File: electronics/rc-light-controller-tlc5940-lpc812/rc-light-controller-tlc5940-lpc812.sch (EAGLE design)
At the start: 41 parts, among them U2 TLC5940PWP

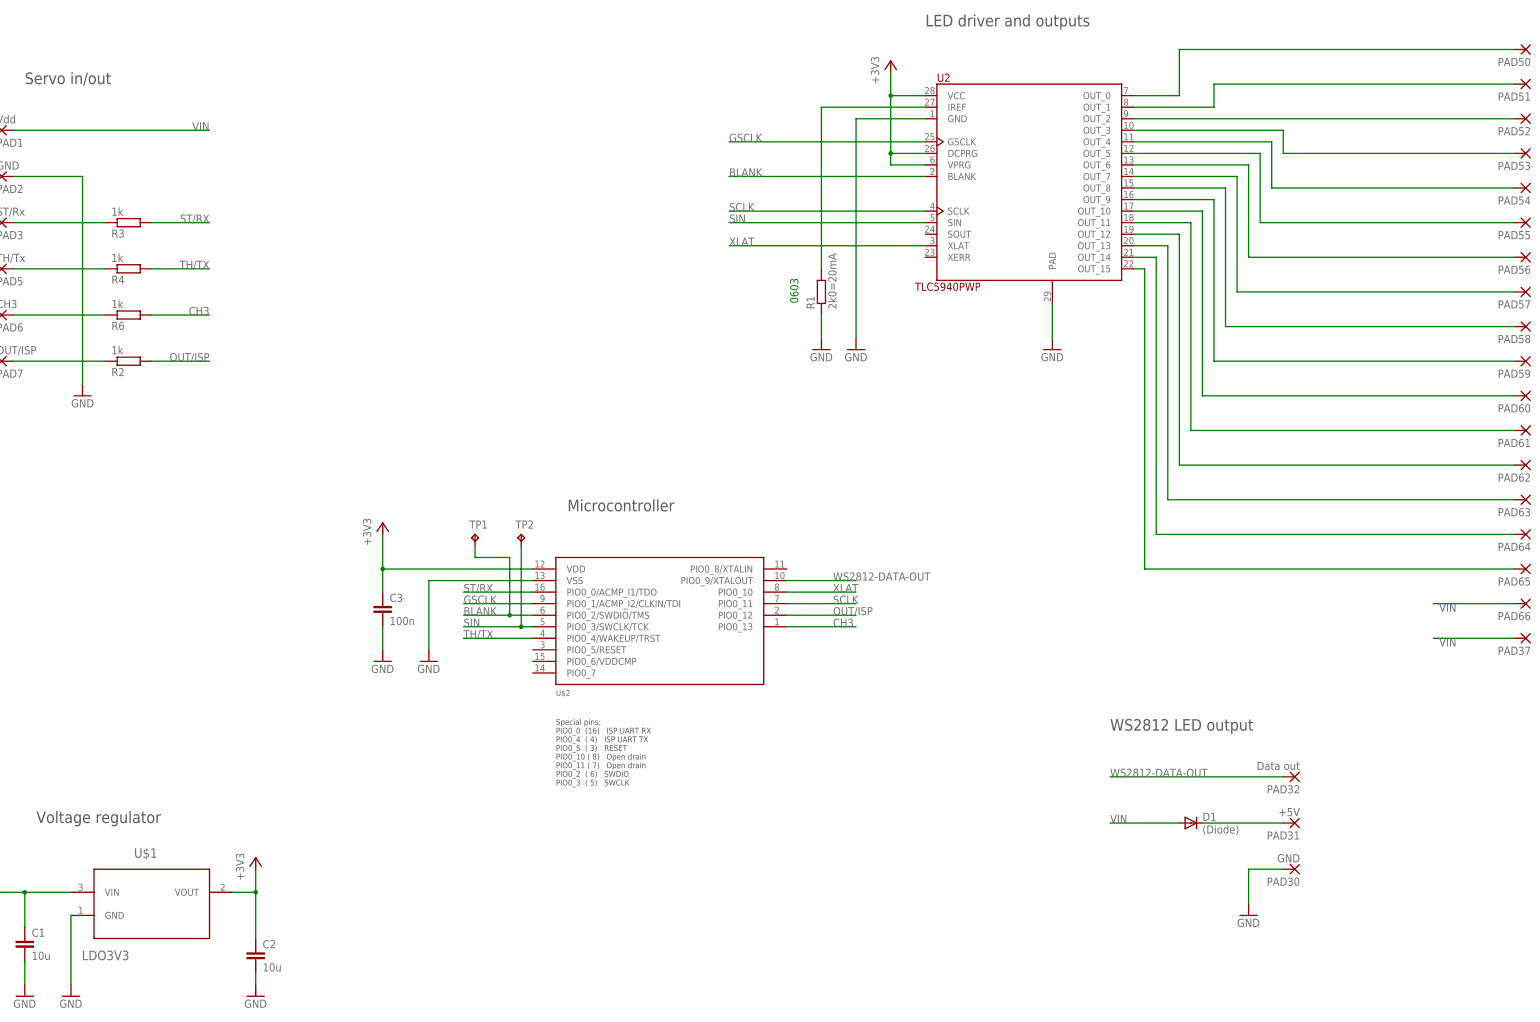
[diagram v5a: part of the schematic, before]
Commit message: Add reset test pad, tweak silk screen and vias
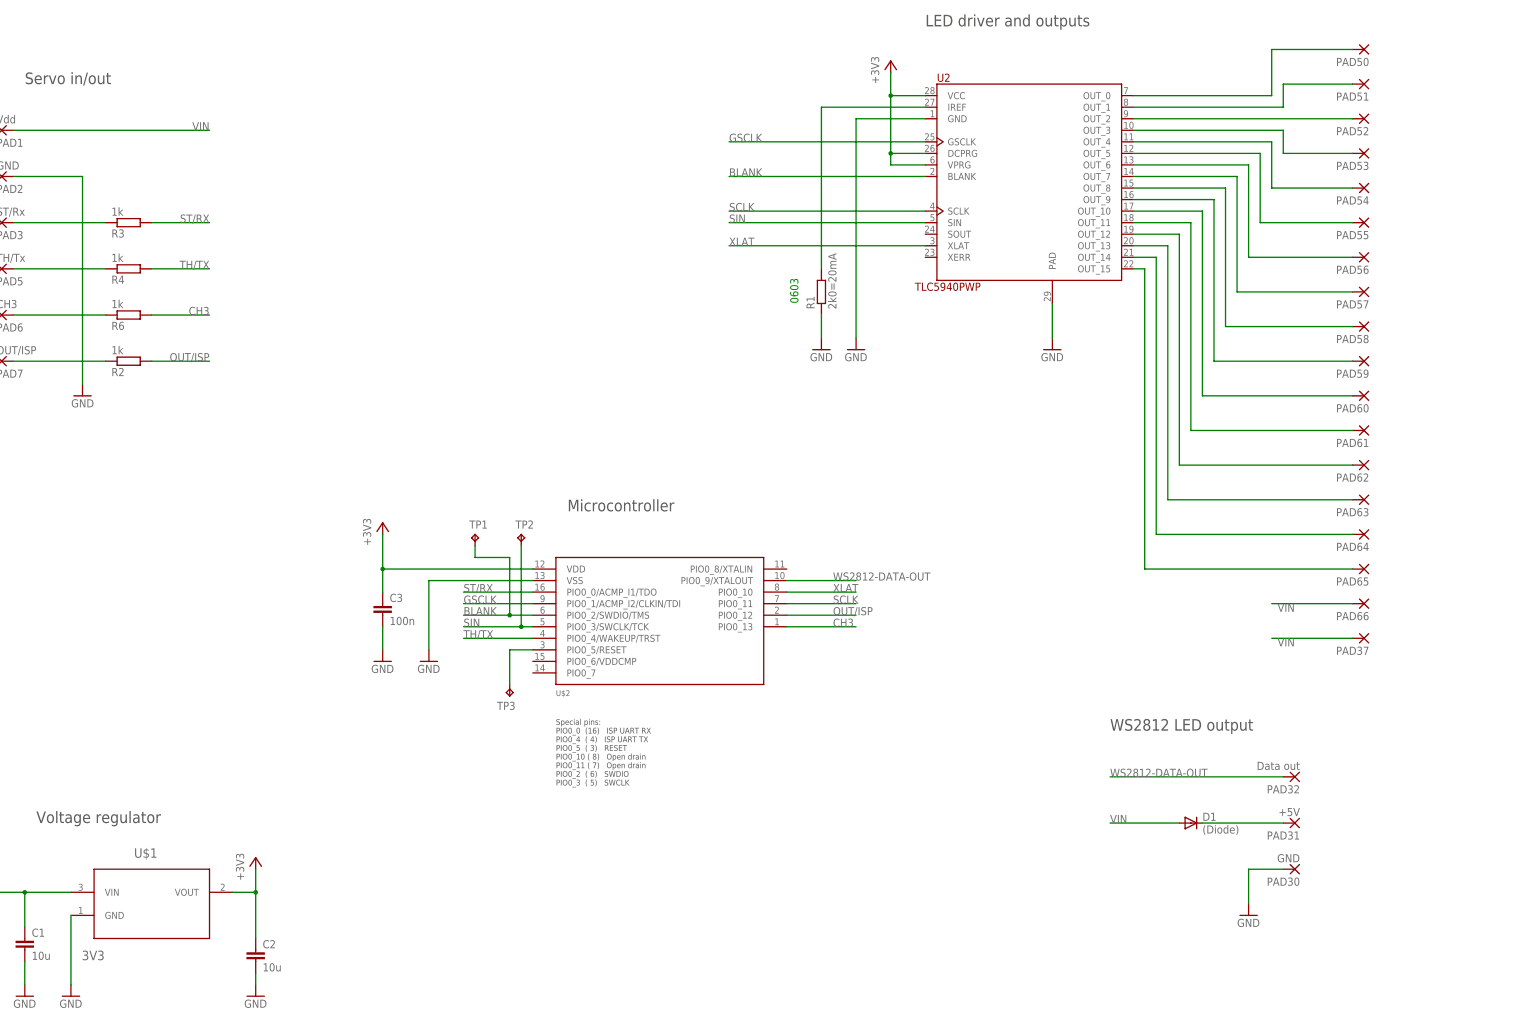
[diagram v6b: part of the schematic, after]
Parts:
- added TP3: RESET, testpad:TPTP10R
- U$1: value LDO3V3 -> 3V3
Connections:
- new net N$4: TP3.TP, U$2.PIO0_5/RESET
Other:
- moved on the sheet: PAD37, PAD50, PAD51, PAD52, PAD53, PAD54, PAD55, PAD56, PAD57, PAD58, PAD59, PAD60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

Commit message: Update board pin assignment to avoid using open drain pins
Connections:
- net BLANK: now also U$2.PIO0_6/VDDCMP; no longer TP1.TP, U$2.PIO0_2/SWDIO/TMS
- net SCLK: now also TP2.TP, U$2.PIO0_3/SWCLK/TCK; no longer U$2.PIO0_11
- net SIN: now also U$2.PIO0_7; no longer TP2.TP, U$2.PIO0_3/SWCLK/TCK
- net XLAT: now also TP1.TP, U$2.PIO0_2/SWDIO/TMS; no longer U$2.PIO0_10
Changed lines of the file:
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@@
 </segment>
 <segment>
-<pinref part="U$2" gate="G$1" pin="PIO0_3/SWCLK/TCK"/>
-<wire x1="152.4" y1="114.3" x2="149.86" y2="114.3" width="0.1524" layer="91"/>
-<label x="137.16" y="114.3" size="1.778" layer="95"/>
-<wire x1="149.86" y1="114.3" x2="137.16" y2="114.3" width="0.1524" layer="91"/>
-<wire x1="149.86" y1="114.3" x2="149.86" y2="132.08" width="0.1524" layer="91"/>
-<junction x="149.86" y="114.3"/>
-<pinref part="TP2" gate="G$1" pin="TP"/>
+<wire x1="152.4" y1="104.14" x2="137.16" y2="104.14" width="0.1524" layer="91"/>
+<label x="137.16" y="104.14" size="1.778" layer="95"/>
+<pinref part="U$2" gate="G$1" pin="PIO0_7"/>
 </segment>
 </net>
@@
 </segment>
 <segment>
-<wire x1="208.28" y1="119.38" x2="223.52" y2="119.38" width="0.1524" layer="91"/>
-<pinref part="U$2" gate="G$1" pin="PIO0_11"/>
-<label x="218.44" y="119.38" size="1.778" layer="95"/>
+<label x="137.16" y="114.3" size="1.778" layer="95"/>
+<wire x1="149.86" y1="114.3" x2="137.16" y2="114.3" width="0.1524" layer="91"/>
+<pinref part="U$2" gate="G$1" pin="PIO0_3/SWCLK/TCK"/>
+<wire x1="152.4" y1="114.3" x2="149.86" y2="114.3" width="0.1524" layer="91"/>
+<wire x1="149.86" y1="114.3" x2="149.86" y2="132.08" width="0.1524" layer="91"/>
+<pinref part="TP2" gate="G$1" pin="TP"/>
+<junction x="149.86" y="114.3"/>
 </segment>
 </net>
 <net name="XLAT" class="0">
 <segment>
-<pinref part="U$2" gate="G$1" pin="PIO0_10"/>
-<wire x1="208.28" y1="121.92" x2="223.52" y2="121.92" width="0.1524" layer="91"/>
-<label x="218.44" y="121.92" size="1.778" layer="95"/>
+<label x="137.16" y="116.84" size="1.778" layer="95"/>
+<wire x1="147.32" y1="116.84" x2="137.16" y2="116.84" width="0.1524" layer="91"/>
+<pinref part="U$2" gate="G$1" pin="PIO0_2/SWDIO/TMS"/>
+<wire x1="152.4" y1="116.84" x2="147.32" y2="116.84" width="0.1524" layer="91"/>
+<wire x1="147.32" y1="116.84" x2="147.32" y2="129.54" width="0.1524" layer="91"/>
+<pinref part="TP1" gate="G$1" pin="TP"/>
+<wire x1="147.32" y1="129.54" x2="139.7" y2="129.54" width="0.1524" layer="91"/>
+<wire x1="139.7" y1="129.54" x2="139.7" y2="132.08" width="0.1524" layer="91"/>
+<junction x="147.32" y="116.84"/>
 </segment>
 <segment>
@@
 </segment>
 <segment>
-<pinref part="U$2" gate="G$1" pin="PIO0_2/SWDIO/TMS"/>
-<wire x1="152.4" y1="116.84" x2="147.32" y2="116.84" width="0.1524" layer="91"/>
-<label x="137.16" y="116.84" size="1.778" layer="95"/>
-<wire x1="147.32" y1="116.84" x2="137.16" y2="116.84" width="0.1524" layer="91"/>
-<wire x1="147.32" y1="116.84" x2="147.32" y2="129.54" width="0.1524" layer="91"/>
-<junction x="147.32" y="116.84"/>
-<pinref part="TP1" gate="G$1" pin="TP"/>
-<wire x1="147.32" y1="129.54" x2="139.7" y2="129.54" width="0.1524" layer="91"/>
-<wire x1="139.7" y1="129.54" x2="139.7" y2="132.08" width="0.1524" layer="91"/>
+<wire x1="152.4" y1="106.68" x2="137.16" y2="106.68" width="0.1524" layer="91"/>
+<label x="137.16" y="106.68" size="1.778" layer="95"/>
+<pinref part="U$2" gate="G$1" pin="PIO0_6/VDDCMP"/>
 </segment>
 </net>

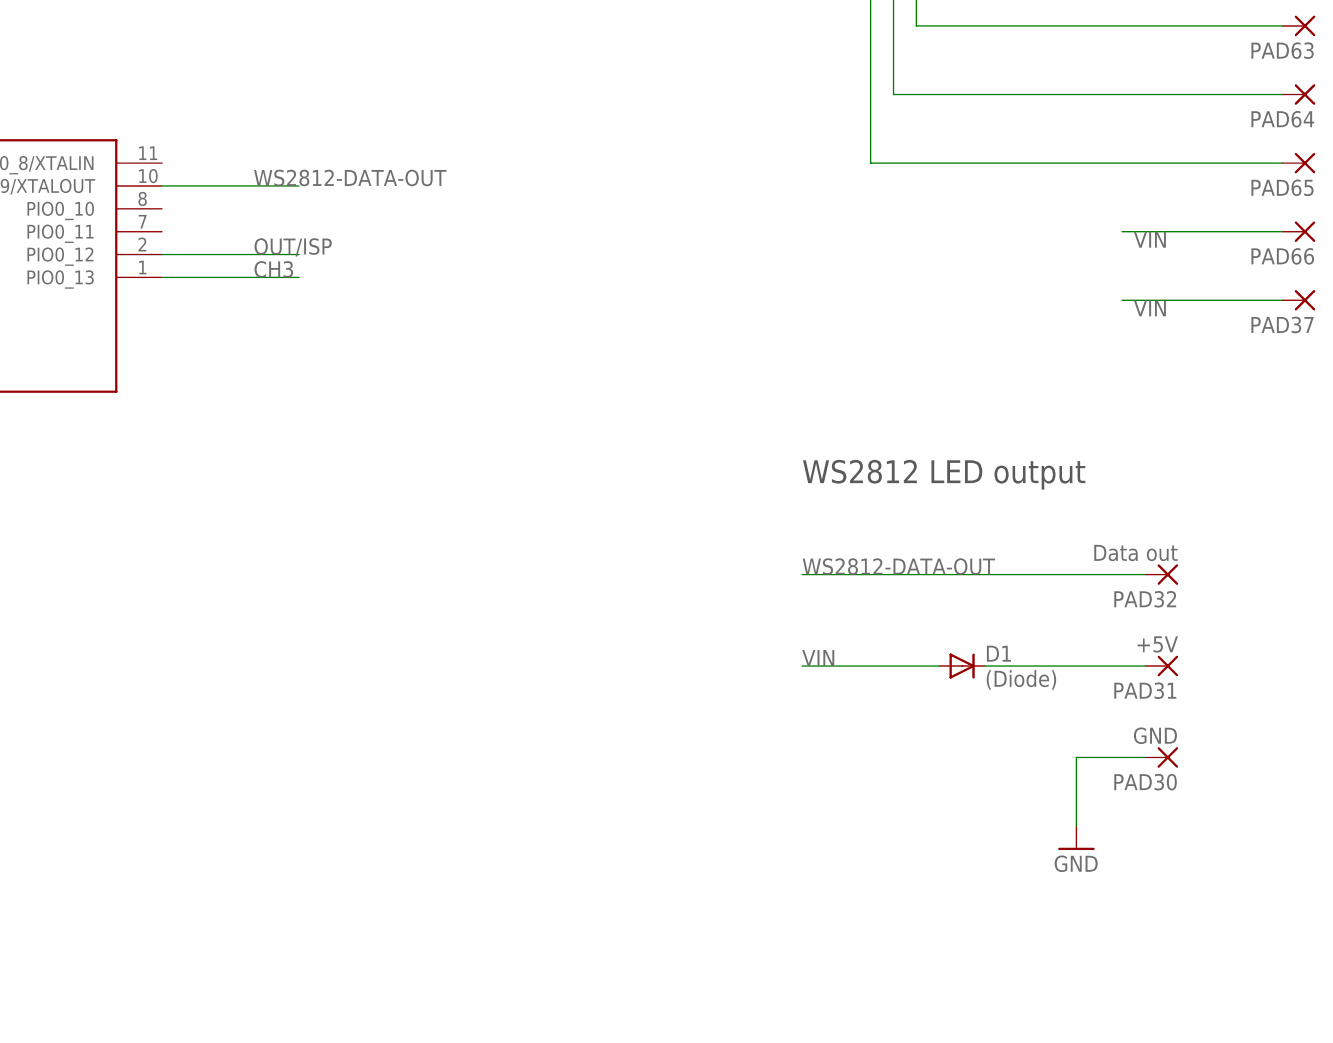
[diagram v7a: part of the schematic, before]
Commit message: Remove WS2812 support
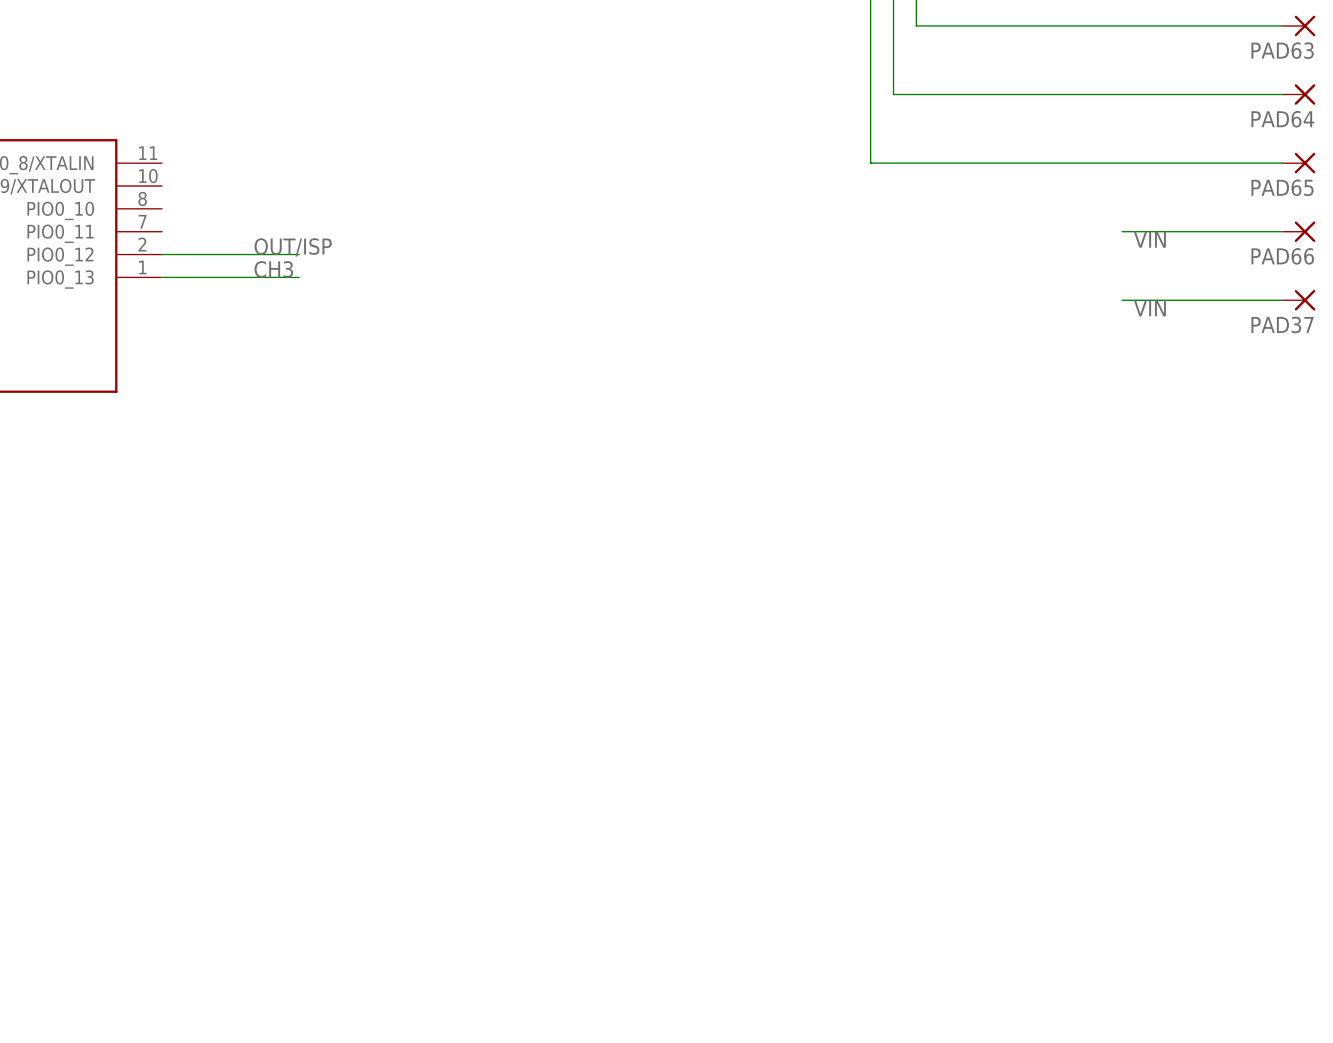
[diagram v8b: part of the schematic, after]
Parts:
- removed D1: (Diode), diode:ES2D
- removed PAD30: GND, wirepad:SDM80X120
- removed PAD31: +5V, wirepad:SDM80X120
- removed PAD32: Data out, wirepad:SDM80X120
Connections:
- removed net N$3: D1.C, PAD31.P
- removed net WS2812-DATA-OUT: PAD32.P, U$2.PIO0_9/XTALOUT
- net GND: no longer PAD30.P
- net VIN: no longer D1.A
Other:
- note removed: "WS2812 LED output"
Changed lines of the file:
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@@
 <part name="PAD6" library="wirepad" deviceset="SDM80X120" device="" value="CH3"/>
 <part name="R6" library="rcl" deviceset="R-EU_" device="R0603" value="1k"/>
-<part name="D1" library="diode" deviceset="ES2D" device="" value="(Diode)"/>
-<part name="PAD30" library="wirepad" deviceset="SDM80X120" device="" value="GND"/>
-<part name="PAD31" library="wirepad" deviceset="SDM80X120" device="" value="+5V"/>
-<part name="PAD32" library="wirepad" deviceset="SDM80X120" device="" value="Data out"/>
-<part name="GND9" library="supply1" deviceset="GND" device=""/>
 <part name="FRAME1" library="frames" deviceset="A3L-LOC" device=""/>
 <part name="R2" library="rcl" deviceset="R-EU_" device="R0603" value="1k"/>
@@
 <text x="43.18" y="71.12" size="2.54" layer="97">Voltage regulator</text>
 <text x="160.02" y="139.7" size="2.54" layer="97">Microcontroller</text>
-<text x="279.4" y="91.44" size="2.54" layer="97">WS2812 LED output</text>
 </plain>
 <instances>
@@
 <instance part="PAD6" gate="G$1" x="35.56" y="182.88" rot="MR180"/>
 <instance part="R6" gate="G$1" x="63.5" y="182.88" rot="MR180"/>
-<instance part="D1" gate="G$1" x="297.18" y="71.12"/>
-<instance part="PAD30" gate="G$1" x="320.04" y="60.96" rot="R180"/>
-<instance part="PAD31" gate="G$1" x="320.04" y="71.12" rot="R180"/>
-<instance part="PAD32" gate="G$1" x="320.04" y="81.28" rot="R180"/>
-<instance part="GND9" gate="1" x="309.88" y="50.8"/>
 <instance part="FRAME1" gate="G$1" x="0" y="0" smashed="yes">
 <attribute name="DRAWING_NAME" x="344.17" y="15.24" size="1.27" layer="94" font="vector" ratio="10"/>
@@
 <wire x1="266.7" y1="185.42" x2="266.7" y2="177.8" width="0.1524" layer="91"/>
 </segment>
-<segment>
-<pinref part="PAD30" gate="G$1" pin="P"/>
-<pinref part="GND9" gate="1" pin="GND"/>
-<wire x1="317.5" y1="60.96" x2="309.88" y2="60.96" width="0.1524" layer="91"/>
-<wire x1="309.88" y1="60.96" x2="309.88" y2="53.34" width="0.1524" layer="91"/>
-</segment>
 </net>
 <net name="SIN" class="0">
@@
 </segment>
 <segment>
-<pinref part="D1" gate="G$1" pin="A"/>
-<wire x1="294.64" y1="71.12" x2="279.4" y2="71.12" width="0.1524" layer="91"/>
-<label x="279.4" y="71.12" size="1.778" layer="95"/>
-</segment>
-<segment>
 <wire x1="332.74" y1="111.76" x2="314.96" y2="111.76" width="0.1524" layer="91"/>
 <pinref part="PAD37" gate="1" pin="P"/>
@@
 </segment>
 </net>
-<net name="N$3" class="0">
-<segment>
-<pinref part="PAD31" gate="G$1" pin="P"/>
-<wire x1="299.72" y1="71.12" x2="317.5" y2="71.12" width="0.1524" layer="91"/>
-<pinref part="D1" gate="G$1" pin="C"/>
-</segment>
-</net>
-<net name="WS2812-DATA-OUT" class="0">
-<segment>
-<pinref part="PAD32" gate="G$1" pin="P"/>
-<wire x1="317.5" y1="81.28" x2="279.4" y2="81.28" width="0.1524" layer="91"/>
-<label x="279.4" y="81.28" size="1.778" layer="95"/>
-</segment>
-<segment>
-<pinref part="U$2" gate="G$1" pin="PIO0_9/XTALOUT"/>
-<wire x1="223.52" y1="124.46" x2="208.28" y2="124.46" width="0.1524" layer="91"/>
-<label x="218.44" y="124.46" size="1.778" layer="95"/>
-</segment>
-</net>
